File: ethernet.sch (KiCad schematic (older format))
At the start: 4 parts

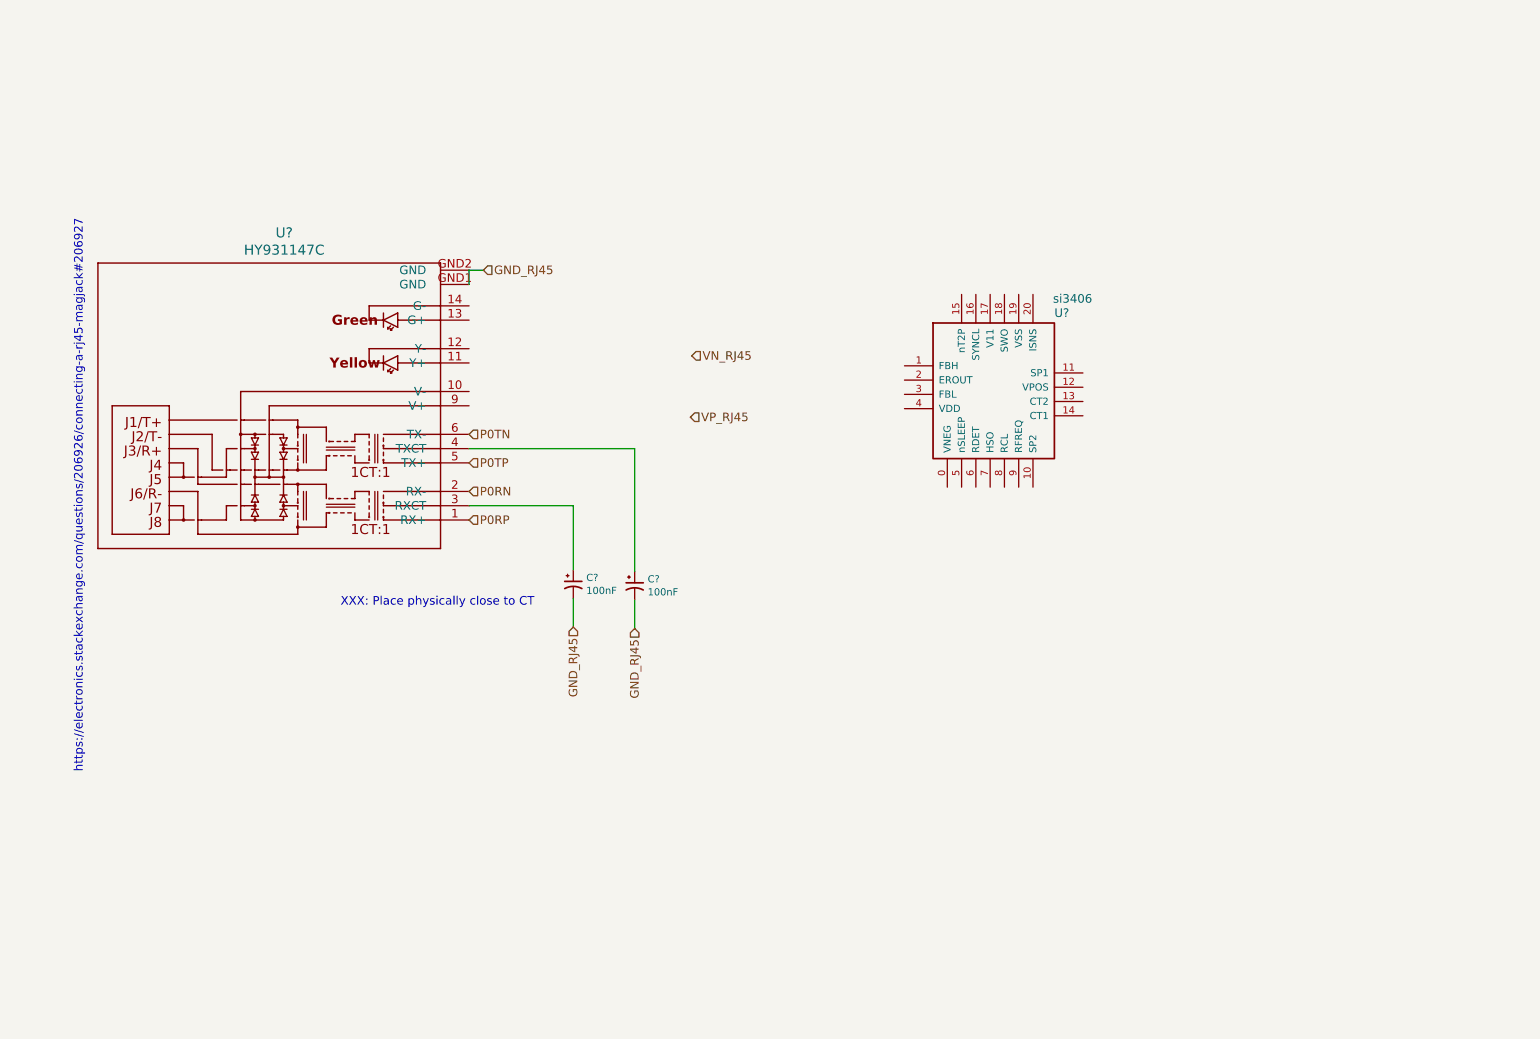
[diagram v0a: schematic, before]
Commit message: Add all POE logic with the si3404, schematic almost finished.
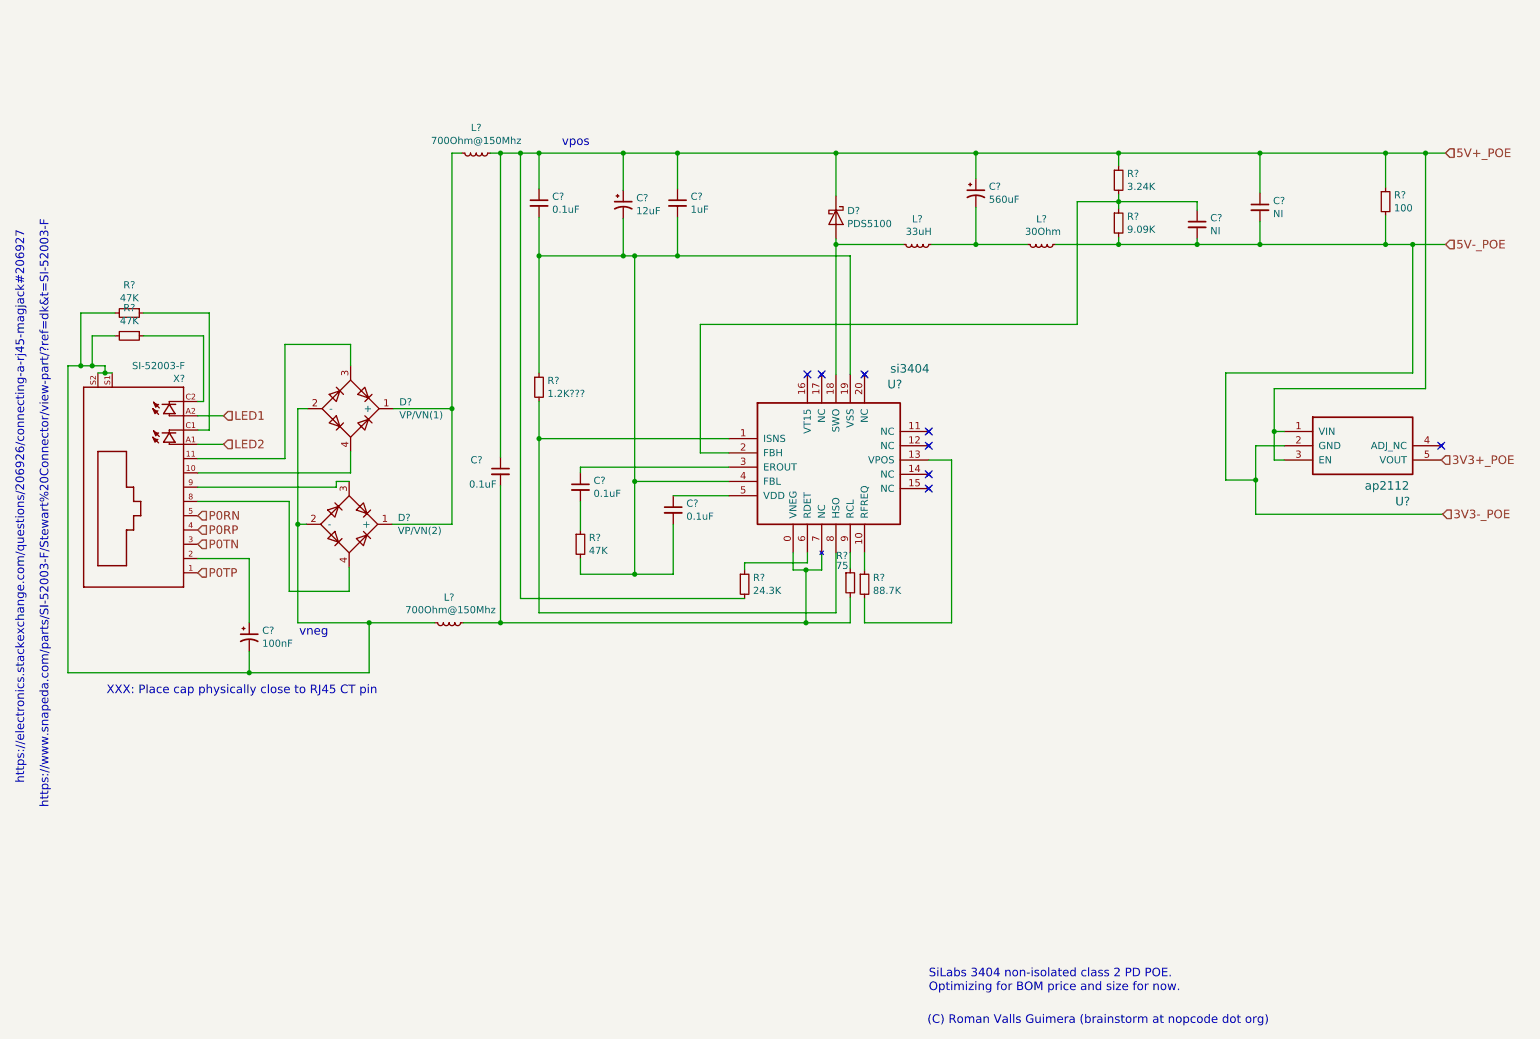
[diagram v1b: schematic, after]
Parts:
- removed C?: 100nF, symbol CP1_Small
- removed U?: HY931147C, symbol HY931147C
- removed U?: si3406, symbol si3406
- added C? (x4): 0.1uF, symbol C_Small
- added C?: 1uF, symbol C_Small
- added C?: 12uF, symbol CP1_Small
- added C?: 560uF, symbol CP1_Small
- added C? (x2): NI, symbol C_Small
- added D?: PDS5100, symbol D_Schottky
- added D?: VP/VN(1), symbol D_Bridge_+-AA
- added D?: VP/VN(2), symbol D_Bridge_+-AA
- added L? (x2): 700Ohm@150Mhz, symbol L_Small
- added L?: 33uH, symbol L_Small
- added L?: 30Ohm, symbol L_Small
- added R?: 3.24K, symbol R_Small
- added R?: 9.09K, symbol R_Small
- added R?: 88.7K, symbol R_Small
- added R?: 75, symbol R_Small
- added R?: 24.3K, symbol R_Small
- added R?: 1.2K???, symbol R_Small
- added R?: 100, symbol R_Small
- added R? (x3): 47K, symbol R_Small
- added U?: si3404, KiCad/Housings_DFN_QFN.pretty:QFN-20-1EP_4x4mm_Pitch0.5mm, symbol si3404
- added U?: ap2112, symbol ap2112
- added X?: SI-52003-F, SI-52003-F, symbol SI-52003-F
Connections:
- net P0RN: now also X?.5 (RD-)
- net P0RP: now also X?.4 (RD+)
- net P0TN: now also X?.3 (TD-)
- net P0TP: now also X?.1 (TD+)
- net at C?.1: now also X?.2 (CT)
- net GND_RJ45: no longer names the net of C?.2
- net GND_RJ45: now also D?.2 (-), D?.2 (-), L?.2, R?.2, R?.2, X?.S1, X?.S2
- new net: C?.2, L?.1, R?.2, U?.0 (VNEG), U?.7 (NC)
- new net: R?.2, U?.1 (ISNS), U?.8 (HSO)
- new net: R?.1, U?.10 (RFREQ)
- new net: R?.2, U?.13 (VPOS)
- new net: D?.2 (A), L?.2, U?.18 (SWO)
- new net: C?.2, C?.2, C?.2, C?.2, R?.1, R?.2, U?.19 (VSS), U?.4 (FBL)
- new net: C?.1, U?.3 (EROUT)
- new net: C?.1, U?.5 (VDD)
- new net: R?.1, U?.6 (RDET)
- new net: R?.1, U?.9 (RCL)
- new net: D?.4, X?.10 (VC2+)
- new net: D?.3, X?.11 (VC2-)
- new net: D?.4, X?.8 (VC1+)
- new net: D?.3, X?.9 (VC1-)
- new net: R?.1, X?.C1
- new net: R?.1, X?.C2
- new net: D?.1 (+), D?.1 (+), L?.2
- new net: C?.2, L?.1, L?.2
- new net: C?.1, R?.1, R?.2
- new net: C?.2, R?.1
- new net 3V3+_POE: U?.5 (VOUT)
- new net 3V3-_POE: C?.2, C?.2, L?.1, R?.2, R?.2, U?.2 (GND)
- new net 5V+_POE: C?.1, C?.1, C?.1, C?.1, C?.1, C?.1, D?.1 (K), L?.1, R?.1, R?.1, R?.2, U?.1 (VIN), U?.3 (EN)
- new net LED1: X?.A2
- new net LED2: X?.A1
- no-connect marks 0 -> 8
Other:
- note added: "(C) Roman Valls Guimera (brainstorm at nopcode dot org)"
- note added: "SiLabs 3404 non-isolated class 2 PD POE.\nOptimizing for BOM price and size for now."
- note added: "XXX: Place cap physically close to RJ45 CT pin"
- note added: "https://www.snapeda.com/parts/SI-52003-F/Stewart%20Connector/view-part/?ref=dk&t=SI-52003-F"
- note added: "vneg"
- note added: "vpos"
- note removed: "XXX: Place physically close to CT"
- moved on the sheet: C?

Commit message: Rearrange components, validate package sizes, think about power plane placement since the ref design is 4 layers... can I add snubbers and other filtering and avoid 4-layer design?
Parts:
- removed C?: 1uF, symbol C_Small
- C1: renamed from C?; value 100nF -> 100nF/100V; footprint (none) -> KiCad/Capacitors_ThroughHole.pretty:CP_Radial_D6.3mm_P2.50mm
- C10: renamed from C?; value NI -> 22uF/6.3V; footprint (none) -> KiCad/Capacitors_SMD.pretty:C_0603
- C2, C4, C6: renamed from C?; footprint (none) -> KiCad/Capacitors_SMD.pretty:C_0603
- C3: renamed from C?; value 0.1uF -> 1uF/100V; footprint (none) -> KiCad/Capacitors_SMD.pretty:C_1210
- C5: renamed from C?; value 12uF -> 15uF/160V; footprint (none) -> KiCad/Capacitors_ThroughHole.pretty:CP_Radial_D6.3mm_P2.50mm
- C8: renamed from C?; footprint (none) -> KiCad/Capacitors_ThroughHole.pretty:CP_Radial_D8.0mm_P3.50mm
- C9: renamed from C?; value NI -> 1nF; footprint (none) -> KiCad/Capacitors_SMD.pretty:C_0603
- D1: renamed from D?; footprint (none) -> KiCad/Diodes_SMD.pretty:D_SMC
- D4, D5: renamed from D?; footprint (none) -> KiCad/Socket_Strips.pretty:Socket_Strip_Straight_2x02_Pitch2.00mm_SMD
- FB1, L3: renamed from L?; footprint (none) -> KiCad/Inductors_SMD.pretty:L_1806
- L1, L2: renamed from L?; value 700Ohm@150Mhz -> MPZ1608B471; footprint (none) -> KiCad/Inductors_SMD.pretty:L_1806
- R1, R10, R2, R4, R5, R6, R7, R8, R9: renamed from R?; footprint (none) -> KiCad/Resistors_SMD.pretty:R_0603
- R3: renamed from R?; value 1.2K??? -> 1.2; footprint (none) -> KiCad/Resistors_SMD.pretty:R_0603
- U3: renamed from U?; footprint (none) -> KiCad/TO_SOT_Packages_SMD.pretty:SOT-23-5
- X1: renamed from X?; footprint SI-52003-F -> SI-52003-F:SI-52003-F
- gave numbers to parts that had none: 1
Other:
- note removed: "https://www.snapeda.com/parts/SI-52003-F/Stewart%20Connector/view-part/?ref=dk&t=SI-52003-F"
- moved on the sheet: C1, C10, C2, C3, C4, C5, C6, C8, C9, D1, D4, D5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

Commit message: Correct main coil (from coilcraft) footprint
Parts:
- L3: footprint KiCad/Inductors_SMD.pretty:L_1806 -> KiCad/Inductors_SMD.pretty:L_Neosid_SM-NE127
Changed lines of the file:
@@
 F 0 "L3" V 6692 2640 50  0000 C CNN
 F 1 "33uH" V 6780 2650 50  0000 C CNN
-F 2 "KiCad/Inductors_SMD.pretty:L_1806" H 6870 2640 50  0001 C CNN
+F 2 "KiCad/Inductors_SMD.pretty:L_Neosid_SM-NE127" H 6870 2640 50  0001 C CNN
 F 3 "" H 6870 2640 50  0001 C CNN
 	1    6870 2640

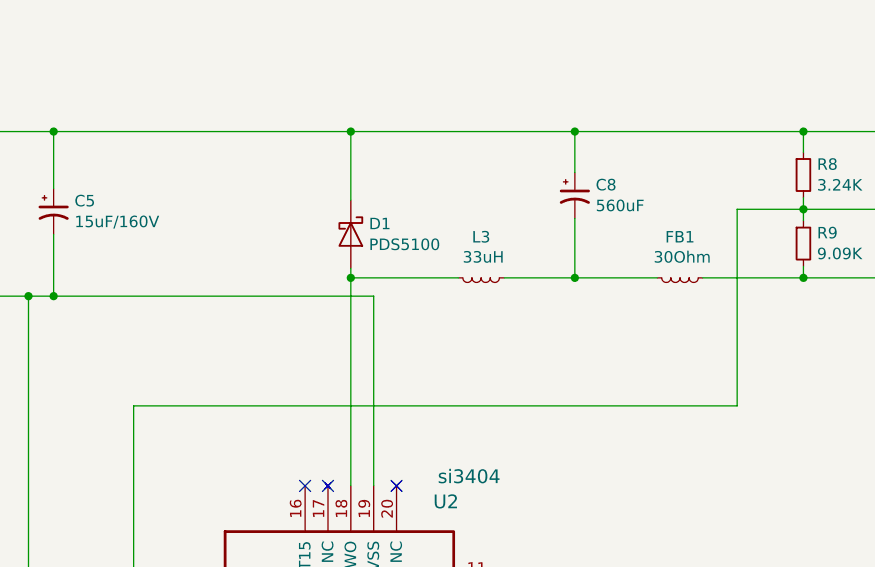
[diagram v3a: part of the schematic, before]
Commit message: Good discussion with Rob Powers about price margins for 2 layer PCB boards vs 4 layer PCBs... no market for that so closing this project and moving to a wESP32-based (or VoCore2) board :-S
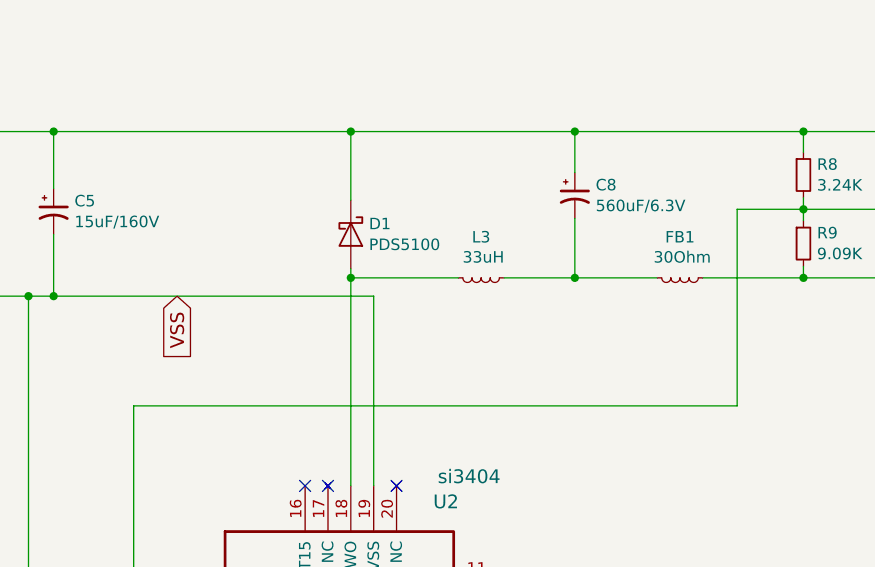
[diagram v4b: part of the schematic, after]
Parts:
- C8: value 560uF -> 560uF/6.3V
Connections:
- net VSS: now reaches C3.2, C5.2, C6.2, R3.1, R4.2, U2.19 (VSS), U2.4 (FBL)
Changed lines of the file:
@@
 P 7280 2280
 F 0 "C8" H 7371 2326 50  0000 L CNN
-F 1 "560uF" H 7371 2235 50  0000 L CNN
+F 1 "560uF/6.3V" H 7371 2235 50  0000 L CNN
 F 2 "KiCad/Capacitors_ThroughHole.pretty:CP_Radial_D8.0mm_P3.50mm" H 7280 2280 50  0001 C CNN
 F 3 "" H 7280 2280 50  0001 C CNN
@@
 	1    0    0    -1
 $EndComp
+Text GLabel 5540 2720 3    60   Input ~ 0
+VSS
 $EndSCHEMATC

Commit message: Migrate to KiCad 5.1 :)
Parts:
- C1, C5, C8: symbol CP1_Small -> device1:CP1_Small
- C10, C2, C3, C4, C6, C9: symbol C_Small -> device1:C_Small
- D1: symbol D_Schottky -> device1:D_Schottky
- D4, D5: symbol D_Bridge_+-AA -> minipcie-eth-rescue:D_Bridge_+-AA
- FB1, L1, L2, L3: symbol L_Small -> device1:L_Small
- R1, R10, R2, R3, R4, R5, R6, R7, R8, R9: symbol R_Small -> device1:R_Small
- U2: symbol si3404 -> si3404:si3404
- U3: symbol ap2112 -> ap2112:ap2112
- X1: symbol SI-52003-F -> SI-52003-F:SI-52003-F
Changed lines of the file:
@@
-EESchema Schematic File Version 3
-LIBS:power
-LIBS:device
-LIBS:transistors
-LIBS:conn
-LIBS:linear
-LIBS:regul
-LIBS:74xx
-LIBS:cmos4000
-LIBS:adc-dac
-LIBS:memory
-LIBS:xilinx
-LIBS:microcontrollers
-LIBS:dsp
-LIBS:microchip
-LIBS:analog_switches
-LIBS:motorola
-LIBS:texas
-LIBS:intel
-LIBS:audio
-LIBS:interface
-LIBS:digital-audio
-LIBS:philips
-LIBS:display
-LIBS:cypress
-LIBS:siliconi
-LIBS:opto
-LIBS:atmel
-LIBS:contrib
-LIBS:valves
-LIBS:win
-LIBS:freetronics_schematic
-LIBS:mpcie
-LIBS:si3406
-LIBS:si3404
-LIBS:SI-52003-F
-LIBS:ap2112
+EESchema Schematic File Version 4
 LIBS:minipcie-eth-cache
-EELAYER 26 0
+EELAYER 29 0
 EELAYER END
 $Descr A4 11693 8268
 encoding utf-8
-Sheet 2 4
+Sheet 2 3
 Title ""
 Date ""
@@
 5V-_POE
 $Comp
-L CP1_Small C1
+L device1:CP1_Small C1
 U 1 1 5BC0DD90
 P 2190 5390
@@
 XXX: Place cap physically close to RJ45 CT pin
 $Comp
-L si3404 U2
+L si3404:si3404 U2
 U 1 1 5BC17319
 P 5350 4000
@@
 $EndComp
 $Comp
-L SI-52003-F X1
+L SI-52003-F:SI-52003-F X1
 U 1 1 5BC18029
 P 1430 4240
@@
 $EndComp
 $Comp
-L L_Small L1
+L device1:L_Small L1
 U 1 1 5BC189F7
 P 3590 5290
@@
 $EndComp
 $Comp
-L L_Small L2
+L device1:L_Small L2
 U 1 1 5BC18B6D
 P 3780 2000
@@
 $EndComp
 $Comp
-L C_Small C3
+L device1:C_Small C3
 U 1 1 5BC18F02
 P 4220 2350
@@
 $EndComp
 $Comp
-L CP1_Small C5
+L device1:CP1_Small C5
 U 1 1 5BC1936F
 P 5000 2350
@@
 $EndComp
 $Comp
-L D_Schottky D1
+L device1:D_Schottky D1
 U 1 1 5BC194B5
 P 6300 2450
@@
 $EndComp
 $Comp
-L L_Small L3
+L device1:L_Small L3
 U 1 1 5BC197D4
 P 6870 2640
@@
 $EndComp
 $Comp
-L CP1_Small C8
+L device1:CP1_Small C8
 U 1 1 5BC19871
 P 7280 2280
@@
 $EndComp
 $Comp
-L R_Small R8
+L device1:R_Small R8
 U 1 1 5BC199BE
 P 8280 2190
@@
 $EndComp
 $Comp
-L R_Small R9
+L device1:R_Small R9
 U 1 1 5BC19AB8
 P 8280 2490
@@
 $EndComp
 $Comp
-L C_Small C10
+L device1:C_Small C10
 U 1 1 5BC19C18
 P 9270 2380
@@
 $EndComp
 $Comp
-L L_Small FB1
+L device1:L_Small FB1
 U 1 1 5BC1A2D1
 P 7740 2640
@@
 $EndComp
 $Comp
-L R_Small R7
+L device1:R_Small R7
 U 1 1 5BC1A6A2
 P 6500 5020
@@
 $EndComp
 $Comp
-L R_Small R6
+L device1:R_Small R6
 U 1 1 5BC1A74D
 P 6400 5010
@@
 $EndComp
 $Comp
-L R_Small R5
+L device1:R_Small R5
 U 1 1 5BC1A7B2
 P 5660 5020
@@
 SiLabs 3404 non-isolated class 2 PD POE.\nOptimizing for BOM price and size for now.
 $Comp
-L C_Small C2
+L device1:C_Small C2
 U 1 1 5BC1DB08
 P 3950 4230
@@
 $EndComp
 $Comp
-L D_Bridge_+-AA D5
+L minipcie-eth-rescue:D_Bridge_+-AA D5
 U 1 1 5BC20810
 P 2900 3790
@@
 $EndComp
 $Comp
-L D_Bridge_+-AA D4
+L minipcie-eth-rescue:D_Bridge_+-AA D4
 U 1 1 5BC20875
 P 2890 4600
@@
 $EndComp
 $Comp
-L R_Small R3
+L device1:R_Small R3
 U 1 1 5BC26899
 P 4220 3640
@@
 $EndComp
 $Comp
-L R_Small R10
+L device1:R_Small R10
 U 1 1 5BC29870
 P 10150 2340
@@
 $EndComp
 $Comp
-L R_Small R4
+L device1:R_Small R4
 U 1 1 5BC2BA83
 P 4510 4740
@@
 $EndComp
 $Comp
-L C_Small C4
+L device1:C_Small C4
 U 1 1 5BC2BAFC
 P 4510 4340
@@
 $EndComp
 $Comp
-L C_Small C6
+L device1:C_Small C6
 U 1 1 5BC2BB7A
 P 5160 4500
@@
 Connection ~ 3030 5290
 $Comp
-L R_Small R2
+L device1:R_Small R2
 U 1 1 5BC3CB58
 P 1350 3280
@@
 $EndComp
 $Comp
-L R_Small R1
+L device1:R_Small R1
 U 1 1 5BC3CBE8
 P 1350 3120
@@
 	2010 4040 1830 4040
 $Comp
-L ap2112 U3
+L ap2112:ap2112 U3
 U 1 1 5BC42283
 P 9440 3950
@@
 	8830 2400 8830 2340
 $Comp
-L C_Small C9
+L device1:C_Small C9
 U 1 1 5BC19B48
 P 8830 2500
